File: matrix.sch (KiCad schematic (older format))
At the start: 142 parts

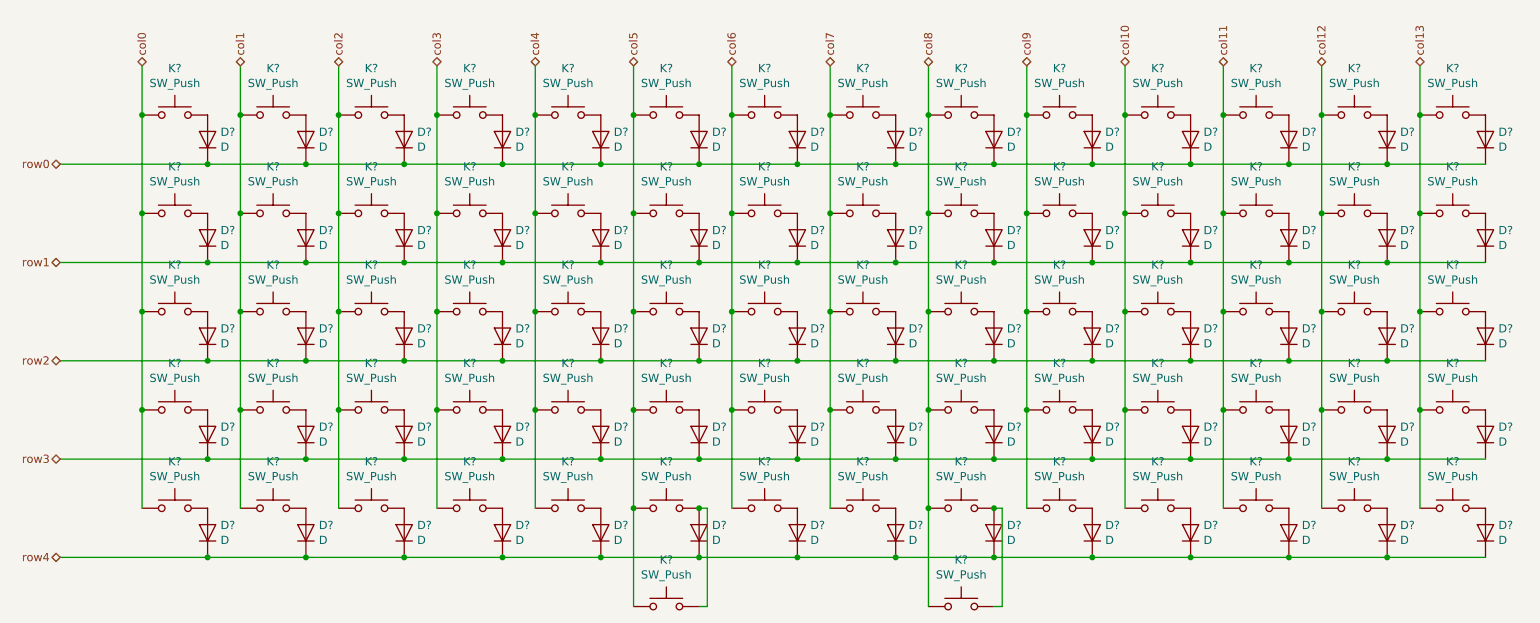
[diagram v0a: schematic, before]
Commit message: Assign PCB footprints to schematic symbols
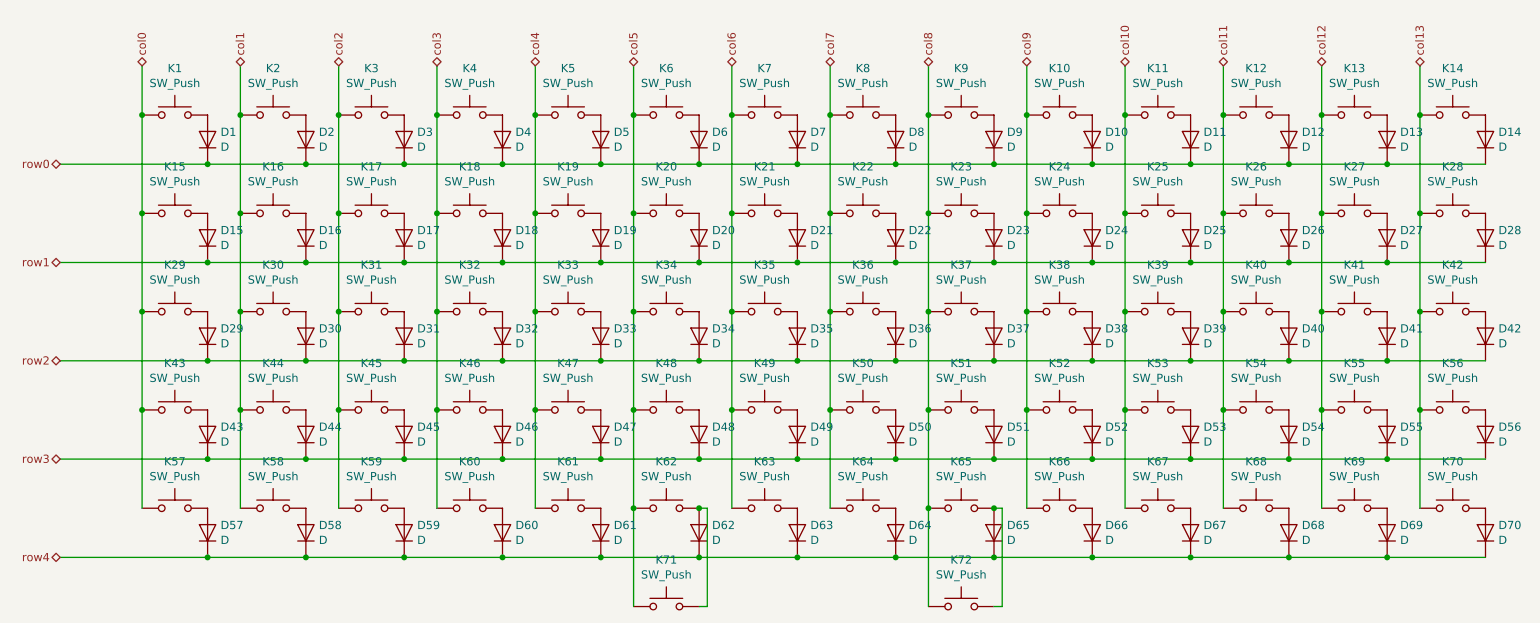
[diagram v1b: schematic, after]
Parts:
- D1, D10, D11, D12, D13, D14, D15, D16, D17, D18, D19, D2, D20, D21, D22, D23, D24, D25, D26, D27, D28, D29, D3, D30, D31, D32, D33, D34, D35, D36, D37, D38, D39, D4, D40, D41, D42, D43, D44, D45, D46, D47, D48, D49, D5, D50, D51, D52, D53, D54, D55, D56, D57, D58, D59, D6, D60, D61, D62, D63, D64, D65, D66, D67, D68, D69, D7, D70, D8, D9: renamed from D?; footprint (none) -> Diode_SMD:D_SOD-123
- K1, K10, K11, K12, K13, K14, K15, K16, K17, K18, K19, K2, K20, K21, K22, K23, K24, K25, K26, K27, K28, K29, K3, K30, K31, K32, K33, K34, K35, K36, K37, K38, K39, K4, K40, K41, K42, K43, K44, K45, K46, K47, K48, K49, K5, K50, K51, K52, K53, K54, K55, K56, K57, K58, K59, K6, K60, K61, K62, K63, K64, K65, K66, K67, K68, K69, K7, K70, K8, K9: renamed from K?; footprint (none) -> MX_Switch:SW_Cherry_MX_1.00u_PCB_Socket
- K71, K72: renamed from K?; footprint (none) -> MX_Switch:SW_Cherry_MX_2.00u_PCB_Socket

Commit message: Replace all MX switch footprint to through-hole solder variant
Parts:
- K1, K10, K11, K12, K13, K14, K15, K16, K17, K18, K19, K2, K20, K21, K22, K23, K24, K25, K26, K27, K28, K29, K3, K30, K31, K32, K33, K34, K35, K36, K37, K38, K39, K4, K40, K41, K42, K43, K44, K45, K46, K47, K48, K49, K5, K50, K51, K52, K53, K54, K55, K56, K57, K58, K59, K6, K60, K61, K62, K63, K64, K65, K66, K67, K68, K69, K7, K70, K8, K9: footprint MX_Switch:SW_Cherry_MX_1.00u_PCB_Socket -> MX_Switch:MX_1.00u_PCB
- K71, K72: footprint MX_Switch:SW_Cherry_MX_2.00u_PCB_Socket -> MX_Switch:MX_2.00u_PCB_ReversedStabilizers

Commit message: Change bottom row to support 6.25u spacebar
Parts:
- added K73: SW_Push, MX_Switch:MX_2.00u_PCB_ReversedStabilizers, symbol Switch:SW_Push
- added K74: SW_Push, MX_Switch:MX_1.00u_PCB, symbol Switch:SW_Push
- K72: footprint MX_Switch:MX_2.00u_PCB_ReversedStabilizers -> MX_Switch:MX_6.25u_PCB_ReversedStabilizers
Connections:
- net col4: now also K71.1
- net col5: now also K72.1; no longer K71.1
- net col6: now also K73.1
- net col8: no longer K72.1
- net col9: now also K74.1
- net at D61.2 (A), K61.2: now also K71.2
- net at D62.2 (A), K62.2: now also K72.2; no longer K71.2
- net at D63.2 (A), K63.2: now also K73.2
- net at D65.2 (A), K65.2: no longer K72.2
- net at D66.2 (A), K66.2: now also K74.2
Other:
- moved on the sheet: K71, K72
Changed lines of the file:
@@
 L Switch:SW_Push K71
 U 1 1 5D189131
-P 4700 4300
-F 0 "K71" H 4700 4585 50  0000 C CNN
-F 1 "SW_Push" H 4700 4494 50  0000 C CNN
-F 2 "MX_Switch:MX_2.00u_PCB_ReversedStabilizers" H 4700 4500 50  0001 C CNN
-F 3 "~" H 4700 4500 50  0001 C CNN
-	1    4700 4300
+P 4100 4300
+F 0 "K71" H 4100 4585 50  0000 C CNN
+F 1 "SW_Push" H 4100 4494 50  0000 C CNN
+F 2 "MX_Switch:MX_2.00u_PCB_ReversedStabilizers" H 4100 4500 50  0001 C CNN
+F 3 "~" H 4100 4500 50  0001 C CNN
+	1    4100 4300
 	1    0    0    -1
 $EndComp
@@
 L Switch:SW_Push K72
 U 1 1 5D19EFD9
-P 6500 4300
-F 0 "K72" H 6500 4585 50  0000 C CNN
-F 1 "SW_Push" H 6500 4494 50  0000 C CNN
-F 2 "MX_Switch:MX_2.00u_PCB_ReversedStabilizers" H 6500 4500 50  0001 C CNN
-F 3 "~" H 6500 4500 50  0001 C CNN
-	1    6500 4300
+P 4700 4300
+F 0 "K72" H 4700 4585 50  0000 C CNN
+F 1 "SW_Push" H 4700 4494 50  0000 C CNN
+F 2 "MX_Switch:MX_6.25u_PCB_ReversedStabilizers" H 4700 4500 50  0001 C CNN
+F 3 "~" H 4700 4500 50  0001 C CNN
+	1    4700 4300
 	1    0    0    -1
 $EndComp
 Wire Wire Line
-	6300 4300 6300 3700
-Connection ~ 6300 3700
+	4300 4300 4350 4300
 Wire Wire Line
-	6700 3700 6750 3700
+	4350 4300 4350 3700
 Wire Wire Line
-	6750 3700 6750 4300
+	4350 3700 4300 3700
+Connection ~ 4300 3700
 Wire Wire Line
-	6750 4300 6700 4300
-Connection ~ 6700 3700
+	3900 4300 3900 3700
+Connection ~ 3900 3700
+Wire Wire Line
+	4900 4300 4950 4300
+Wire Wire Line
+	4950 4300 4950 3700
+Wire Wire Line
+	4950 3700 4900 3700
+Connection ~ 4900 3700
 Wire Wire Line
 	4500 4300 4500 3700
 Connection ~ 4500 3700
+$Comp
+L Switch:SW_Push K73
+U 1 1 5DAE746D
+P 5300 4300
+F 0 "K73" H 5300 4585 50  0000 C CNN
+F 1 "SW_Push" H 5300 4494 50  0000 C CNN
+F 2 "MX_Switch:MX_2.00u_PCB_ReversedStabilizers" H 5300 4500 50  0001 C CNN
+F 3 "~" H 5300 4500 50  0001 C CNN
+	1    5300 4300
+	1    0    0    -1
+$EndComp
 Wire Wire Line
-	4900 3700 4950 3700
+	5100 4300 5100 3700
+Connection ~ 5100 3700
 Wire Wire Line
-	4950 3700 4950 4300
+	5500 4300 5550 4300
 Wire Wire Line
-	4950 4300 4900 4300
-Connection ~ 4900 3700
+	5550 4300 5550 3700
+Wire Wire Line
+	5550 3700 5500 3700
+Connection ~ 5500 3700
+$Comp
+L Switch:SW_Push K74
+U 1 1 5DB0334E
+P 7100 4300
+F 0 "K74" H 7100 4585 50  0000 C CNN
+F 1 "SW_Push" H 7100 4494 50  0000 C CNN
+F 2 "MX_Switch:MX_1.00u_PCB" H 7100 4500 50  0001 C CNN
+F 3 "~" H 7100 4500 50  0001 C CNN
+	1    7100 4300
+	1    0    0    -1
+$EndComp
+Wire Wire Line
+	7300 4300 7350 4300
+Wire Wire Line
+	7350 4300 7350 3700
+Wire Wire Line
+	7350 3700 7300 3700
+Connection ~ 7300 3700
+Wire Wire Line
+	6900 4300 6900 3700
+Connection ~ 6900 3700
 $EndSCHEMATC

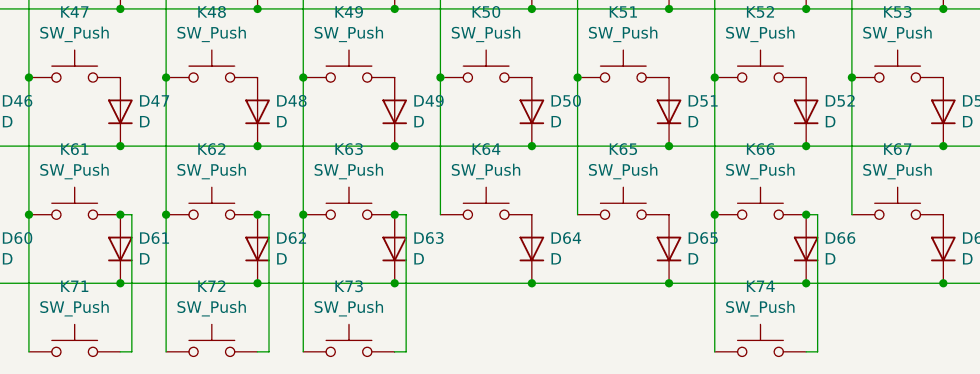
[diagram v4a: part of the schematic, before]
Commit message: Replace 6.25u with 7.00u spacebar support
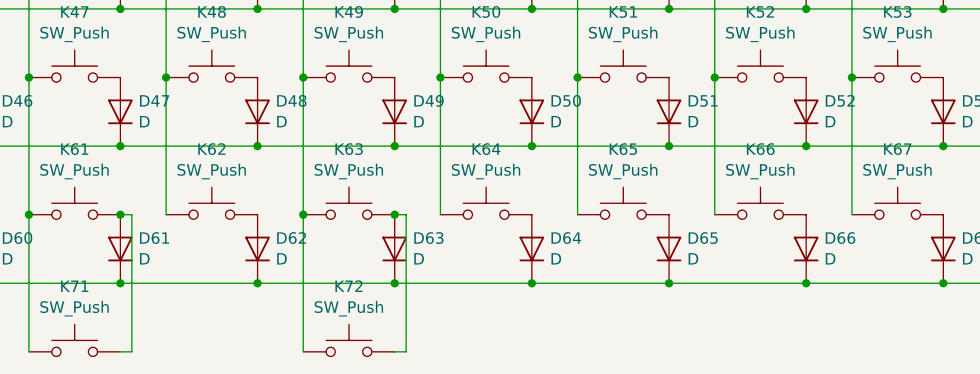
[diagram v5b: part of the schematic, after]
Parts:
- removed K72: SW_Push, MX_Switch:MX_6.25u_PCB_ReversedStabilizers, symbol Switch:SW_Push
- removed K74: SW_Push, MX_Switch:MX_1.00u_PCB, symbol Switch:SW_Push
- K62: footprint MX_Switch:MX_1.00u_PCB -> MX_Switch:MX_7.00u_PCB_ReversedStabilizers
- renumbered K73 to K72
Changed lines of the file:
@@
 F 0 "K62" H 4700 3985 50  0000 C CNN
 F 1 "SW_Push" H 4700 3894 50  0000 C CNN
-F 2 "MX_Switch:MX_1.00u_PCB" H 4700 3900 50  0001 C CNN
+F 2 "MX_Switch:MX_7.00u_PCB_ReversedStabilizers" H 4700 3900 50  0001 C CNN
 F 3 "~" H 4700 3900 50  0001 C CNN
 	1    4700 3700
@@
 	1    0    0    -1
 $EndComp
-$Comp
-L Switch:SW_Push K72
-U 1 1 5D19EFD9
-P 4700 4300
-F 0 "K72" H 4700 4585 50  0000 C CNN
-F 1 "SW_Push" H 4700 4494 50  0000 C CNN
-F 2 "MX_Switch:MX_6.25u_PCB_ReversedStabilizers" H 4700 4500 50  0001 C CNN
-F 3 "~" H 4700 4500 50  0001 C CNN
-	1    4700 4300
-	1    0    0    -1
-$EndComp
 Wire Wire Line
 	4300 4300 4350 4300
@@
 	3900 4300 3900 3700
 Connection ~ 3900 3700
-Wire Wire Line
-	4900 4300 4950 4300
-Wire Wire Line
-	4950 4300 4950 3700
-Wire Wire Line
-	4950 3700 4900 3700
-Connection ~ 4900 3700
-Wire Wire Line
-	4500 4300 4500 3700
-Connection ~ 4500 3700
-$Comp
-L Switch:SW_Push K73
+$Comp
+L Switch:SW_Push K72
 U 1 1 5DAE746D
 P 5300 4300
-F 0 "K73" H 5300 4585 50  0000 C CNN
+F 0 "K72" H 5300 4585 50  0000 C CNN
 F 1 "SW_Push" H 5300 4494 50  0000 C CNN
 F 2 "MX_Switch:MX_2.00u_PCB_ReversedStabilizers" H 5300 4500 50  0001 C CNN
@@
 	5550 3700 5500 3700
 Connection ~ 5500 3700
-$Comp
-L Switch:SW_Push K74
-U 1 1 5DB0334E
-P 7100 4300
-F 0 "K74" H 7100 4585 50  0000 C CNN
-F 1 "SW_Push" H 7100 4494 50  0000 C CNN
-F 2 "MX_Switch:MX_1.00u_PCB" H 7100 4500 50  0001 C CNN
-F 3 "~" H 7100 4500 50  0001 C CNN
-	1    7100 4300
-	1    0    0    -1
-$EndComp
-Wire Wire Line
-	7300 4300 7350 4300
-Wire Wire Line
-	7350 4300 7350 3700
-Wire Wire Line
-	7350 3700 7300 3700
-Connection ~ 7300 3700
-Wire Wire Line
-	6900 4300 6900 3700
-Connection ~ 6900 3700
 $EndSCHEMATC
